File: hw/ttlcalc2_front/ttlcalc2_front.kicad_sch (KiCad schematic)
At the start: 61 parts, among them J1 DISP_CONN, J2 PWR_HV

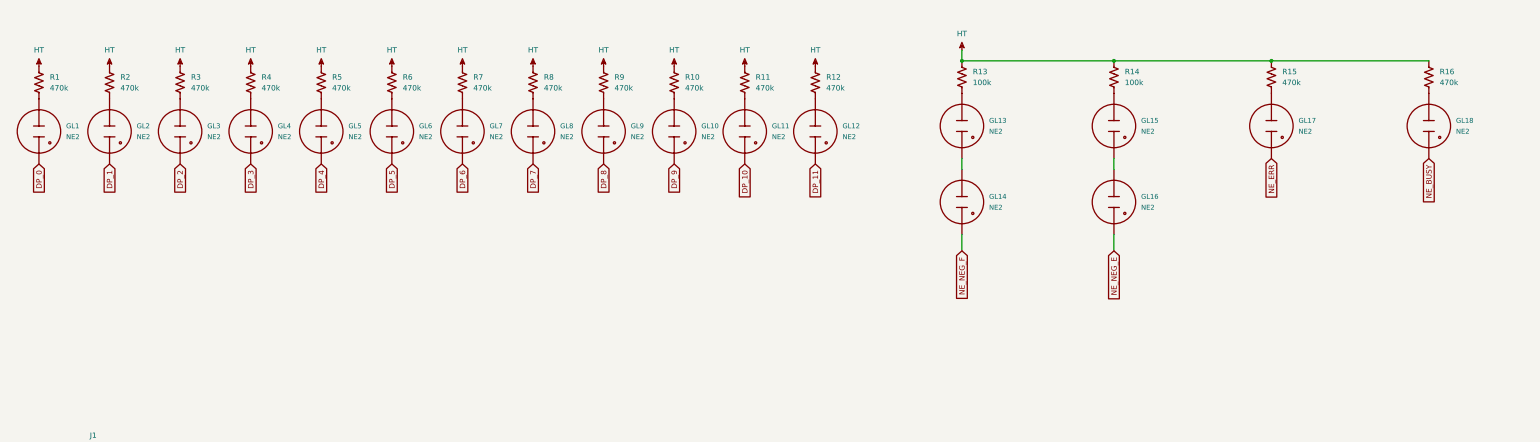
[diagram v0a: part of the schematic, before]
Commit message: Minor display hardware revisions
Add anti-ghosting inter-cathode resistors to nixies
Adjust component values based on experiments
Change from individual netclass labels to rule areas
Tweak traces on display board
Update .gitignore to ignore KiCad lock files
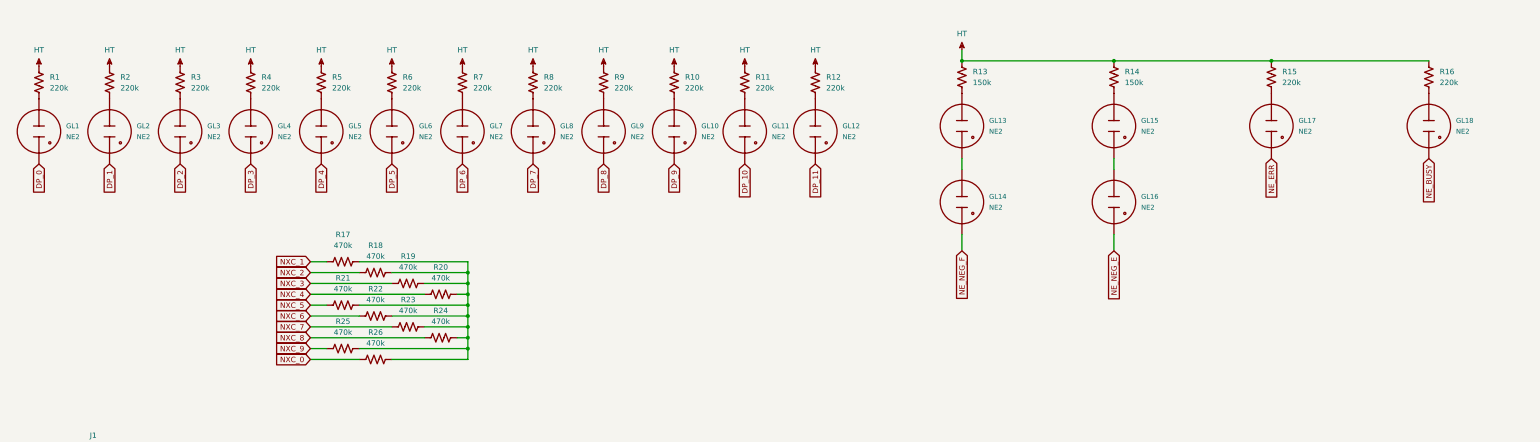
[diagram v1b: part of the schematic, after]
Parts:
- added R17, R18, R19, R20, R21, R22, R23, R24, R25, R26: 470k, Resistor_THT:R_Axial_DIN0207_L6.3mm_D2.5mm_P7.62mm_Horizontal, symbol Device:R_US
- R1, R10, R11, R12, R15, R16, R2, R3, R4, R5, R6, R7, R8, R9: value 470k -> 220k
- R13, R14: value 100k -> 150k
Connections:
- net NXC_0: now also R26.1
- net NXC_1: now also R17.1
- net NXC_2: now also R18.1
- net NXC_3: now also R19.1
- net NXC_4: now also R20.1
- net NXC_5: now also R21.1
- net NXC_6: now also R22.1
- net NXC_7: now also R23.1
- net NXC_8: now also R24.1
- net NXC_9: now also R25.1
- new net: R17.2, R18.2, R19.2, R20.2, R21.2, R22.2, R23.2, R24.2, R25.2, R26.2
